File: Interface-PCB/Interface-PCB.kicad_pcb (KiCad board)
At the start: 2 copper layers, 100 x 100 mm, 69 parts, among them IC1 SN74LVC245AN, IC2 TBD62783APG, IC3 TBD62783APG, J1 BARREL_JACK_PAD, J10 LEVEL_SENSOR, J11 TEMPERATURE_SENSOR, J12 TEMPERATURE_SENSOR, J13 CONN_05JST, J14 CONN_05JST, J2 BARREL_JACK_PAD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

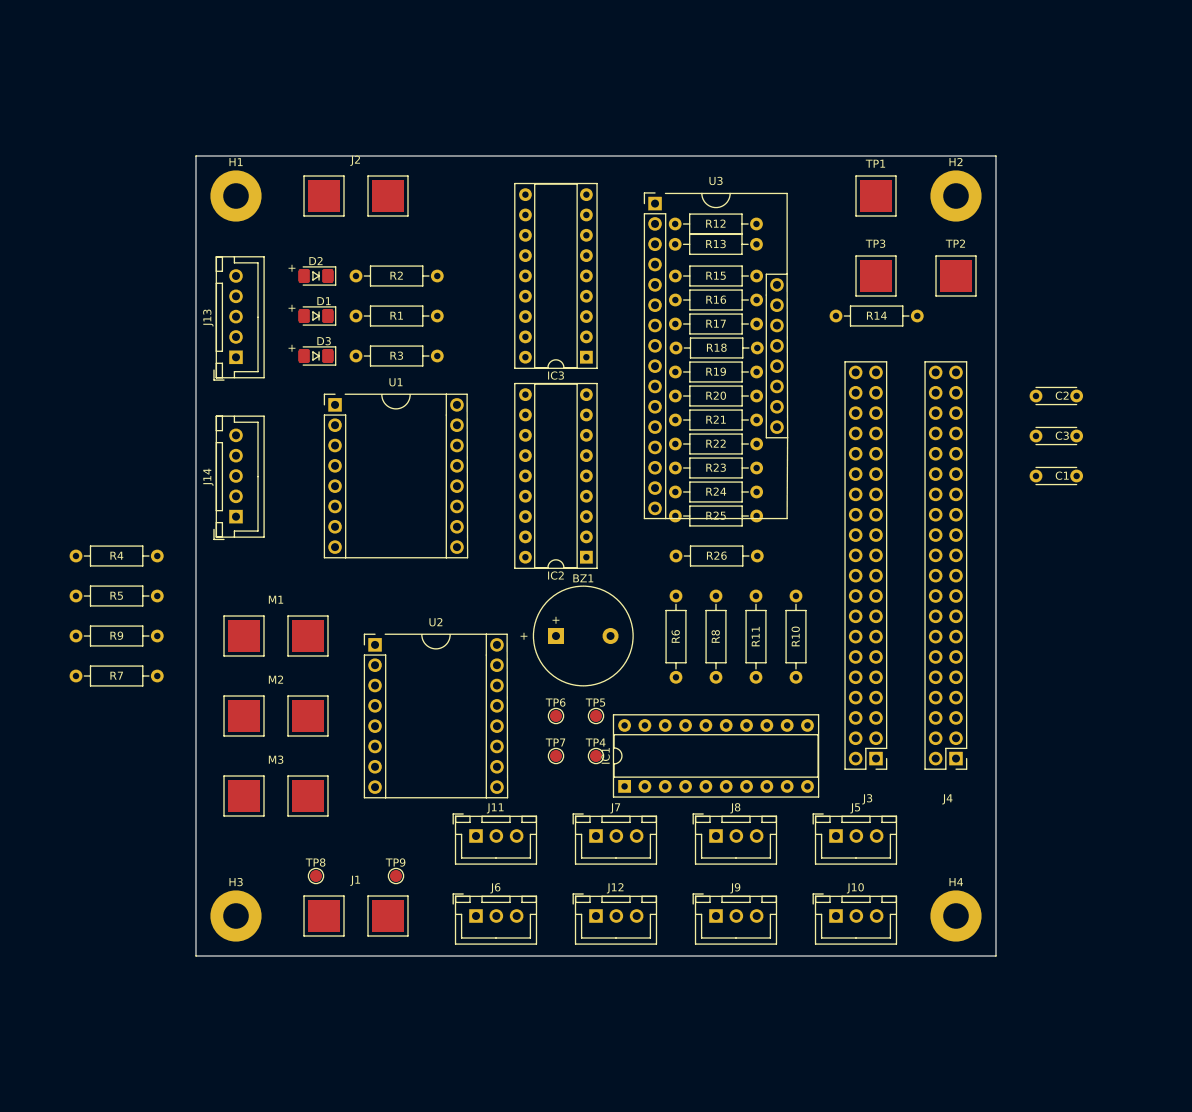
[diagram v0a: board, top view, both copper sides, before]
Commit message: Increase board size, Add connector labels
- Increase board size to 140x130mm
- Refine layout on PCB
- Align breakout board resistors to 2.54mm spacing
- Add Inverted silkscreen labels for off-board connectors
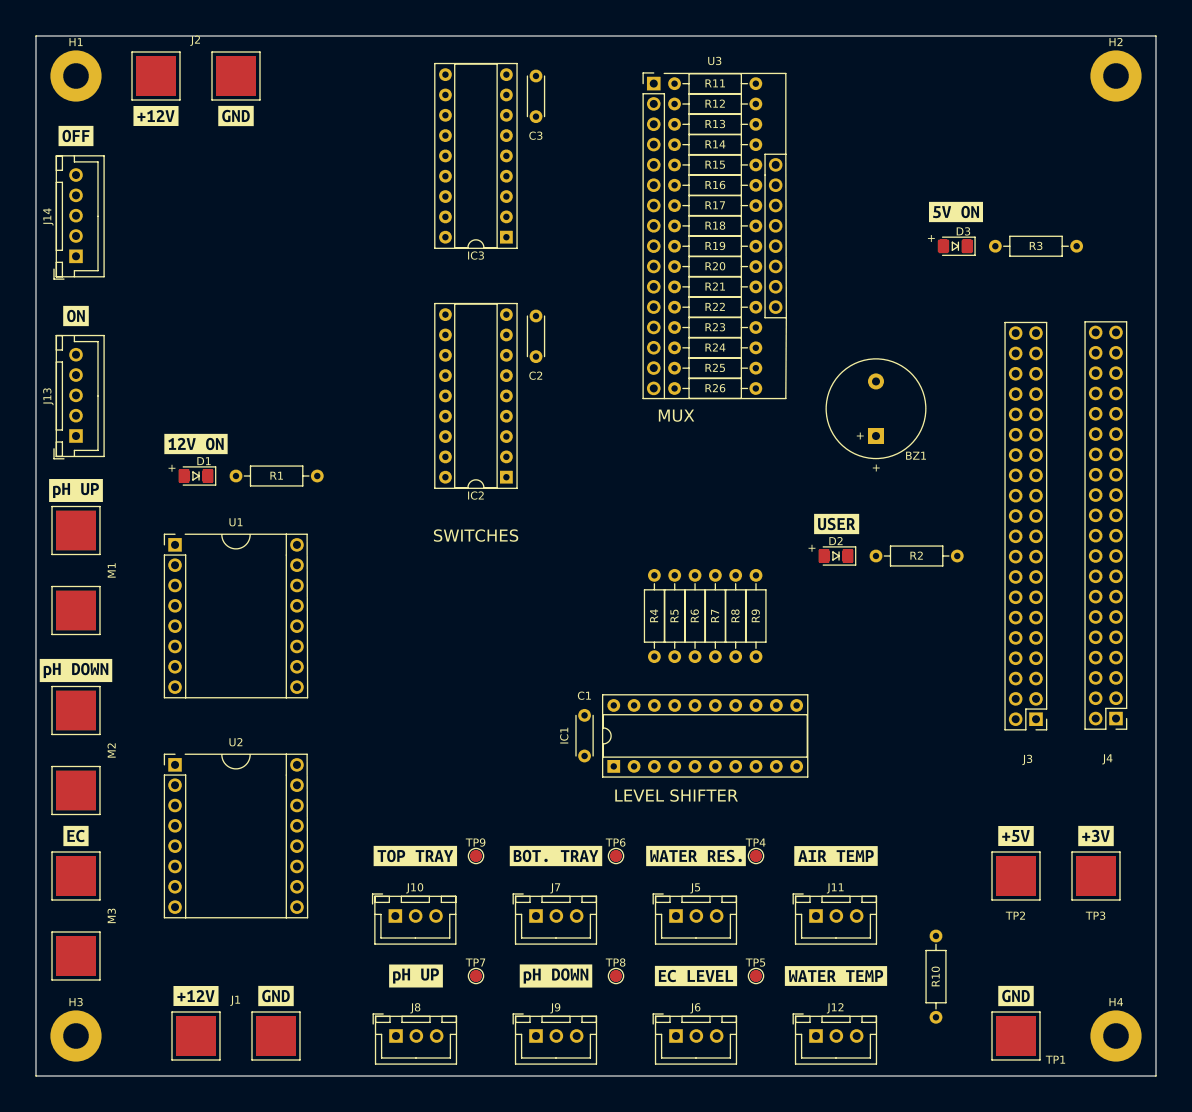
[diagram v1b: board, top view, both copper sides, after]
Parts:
- added kibuzzard-63CB80E4: G***, kibuzzard-63CB80E4, F.Cu at (142.5, 152.5)
- added kibuzzard-63CB8107: G***, kibuzzard-63CB8107, F.Cu at (107.5, 152.5)
- added kibuzzard-63CB8107: G***, kibuzzard-63CB8107, F.Cu at (65.0, 91.8)
- added kibuzzard-63CB811C: G***, kibuzzard-63CB811C, F.Cu at (107.4, 137.5)
- added kibuzzard-63CB8123: G***, kibuzzard-63CB8123, F.Cu at (125.0, 152.5)
- added kibuzzard-63CB8123: G***, kibuzzard-63CB8123, F.Cu at (65.0, 114.3)
- added kibuzzard-63CB8136: G***, kibuzzard-63CB8136, F.Cu at (160.0, 137.5)
- added kibuzzard-63CB813E: G***, kibuzzard-63CB813E, F.Cu at (160.0, 152.5)
- added kibuzzard-63CB8267: G***, kibuzzard-63CB8267, F.Cu at (125.0, 137.5)
- added kibuzzard-63CB83DB: G***, kibuzzard-63CB83DB, F.Cu at (80.0, 86.0)
- added kibuzzard-63CB83FB: G***, kibuzzard-63CB83FB, F.Cu at (175.0, 57.0)
- added kibuzzard-63CB8415: G***, kibuzzard-63CB8415, F.Cu at (160.1, 96.0)
- added kibuzzard-63CB856E: G***, kibuzzard-63CB856E, F.Cu at (65.0, 135.0)
- added kibuzzard-63CB864A: G***, kibuzzard-63CB864A, F.Cu at (182.5, 135.0)
- added kibuzzard-63CB8656: G***, kibuzzard-63CB8656, F.Cu at (192.5, 135.0)
- added kibuzzard-63CB8663: G***, kibuzzard-63CB8663, F.Cu at (182.5, 155.0)
- added kibuzzard-63CB8663: G***, kibuzzard-63CB8663, F.Cu at (90.0, 155.0)
- added kibuzzard-63CB8663: G***, kibuzzard-63CB8663, F.Cu at (85.0, 45.0)
- added kibuzzard-63CB8737: G***, kibuzzard-63CB8737, F.Cu at (80.0, 155.0)
- added kibuzzard-63CB8737: G***, kibuzzard-63CB8737, F.Cu at (75.0, 45.0)
- added kibuzzard-63CB877B: G***, kibuzzard-63CB877B, F.Cu at (142.5, 137.5)
- added kibuzzard-63CB87CD: G***, kibuzzard-63CB87CD, F.Cu at (65.0, 47.5)
- added kibuzzard-63CB87D2: G***, kibuzzard-63CB87D2, F.Cu at (65.0, 70.0)
- J1, J2, M1, M2, M3: footprint AA_Custom_Components:PowerPad_Pair_4.0x4.0mm -> AA_Custom_Components:PowerPad_Pair_5.0x5.0mm
- TP1, TP2, TP3: footprint AA_Custom_Components:TestPoint_Pad_4.0x4.0mm -> AA_Custom_Components:TestPoint_Pad_5.0x5.0mm
- moved TP1 106.4 mm to (182.5, 160.0)
- moved R9 85.0 mm to (150.0, 112.6), turned to 90 degrees
- moved D3 81.1 mm to (174.9, 61.3)
- moved R3 81.1 mm to (179.9, 61.3)
- moved R7 80.9 mm to (144.9, 102.4), turned to -90 degrees
- moved TP3 79.9 mm to (192.5, 140.0)
- moved C3 77.0 mm to (122.5, 40.0), turned to -90 degrees
- moved TP2 75.4 mm to (182.5, 140.0)
- moved R5 74.9 mm to (139.8, 102.4), turned to -90 degrees
- moved D2 73.8 mm to (160.0, 100.0)
- moved R2 73.8 mm to (165.0, 100.0)
- moved R4 73.4 mm to (137.3, 112.6), turned to 90 degrees
- moved C1 66.4 mm to (128.6, 125.0), turned to 90 degrees
- moved R11 64.8 mm to (139.8, 41.0), turned to 0 degrees
- moved C2 63.3 mm to (122.5, 70.0), turned to -90 degrees
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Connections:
- IC1 pad 2: LEVEL_WATER -> LEVEL_TRAY_TOP
- IC1 pad 4: LEVEL_PH_DOWN -> LEVEL_TRAY_BOTTOM
- IC1 pad 5: LEVEL_EC -> LEVEL_PH_DOWN
- IC1 pad 6: LEVEL_TRAY_TOP -> LEVEL_WATER
- IC1 pad 7: LEVEL_TRAY_BOTTOM -> LEVEL_EC
- R4 pad 1: LEVEL_WATER_3V3 -> LEVEL_TRAY_TOP_3V3
- R6 pad 1: LEVEL_PH_DOWN_3V3 -> LEVEL_TRAY_BOTTOM_3V3
- R7 pad 1: LEVEL_EC_3V3 -> LEVEL_PH_DOWN_3V3
- R8 pad 1: LEVEL_TRAY_TOP_3V3 -> LEVEL_WATER_3V3
- R9 pad 1: LEVEL_TRAY_BOTTOM_3V3 -> LEVEL_EC_3V3
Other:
- board size 100 x 100 mm -> 140 x 130 mm
- board text added: "0.1270 mm / 0.1270 mm"
- board text added: "0.2000 mm"
- board text added: "1.6000 mm"
- board text added: "140.0500 mm x 130.0500 mm"
- board text added: "2"
- board text added: "BOARD CHARACTERISTICS"
- board text added: "Board Thickness:"
- board text added: "Board overall dimensions:"
- board text added: "Castellated pads:"
- board text added: "Copper Finish:"
- board text added: "Copper Layer Count:"
- board text added: "Edge card connectors:"
- board text added: "HAL SnPb"
- board text added: "Impedance Control:"
- board text added: "LEVEL SHIFTER"
- board text added: "MUX"
- board text added: "Min hole diameter:"
- board text added: "Min track/spacing:"
- board text added: "No"
- board text added: "Plated Board Edge:"
- board text added: "SWITCHES"

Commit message: Create ground plane, swap motor driver pins
- Create Ground pour/plane on F.Copper
- Swap motor driver pin assignments, to resolve some route
  criss-crossing
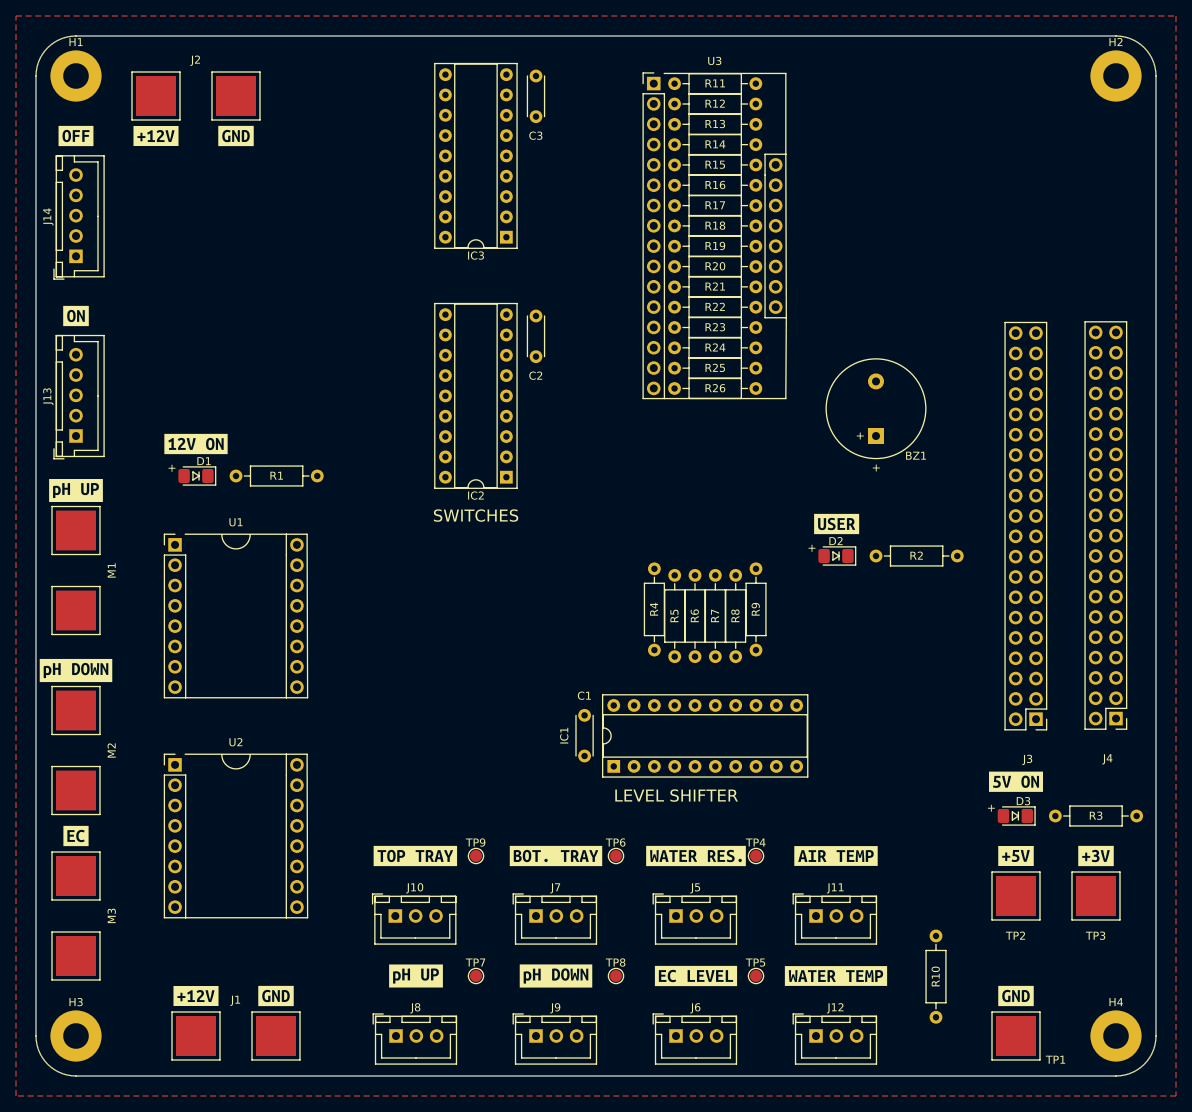
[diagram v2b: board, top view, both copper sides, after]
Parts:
- moved D3 71.6 mm to (182.4, 132.5)
- moved R3 71.6 mm to (187.4, 132.5)
- moved kibuzzard-63CB83FB 71.6 mm to (182.5, 128.2)
- moved R4 11.0 mm to (137.3, 101.6), turned to -90 degrees
- moved R9 11.0 mm to (150.0, 101.6), turned to -90 degrees
- moved J2 2.50 mm to (80.0, 42.5)
- moved TP2 2.50 mm to (182.5, 142.5)
- moved TP3 2.50 mm to (192.5, 142.5)
- moved kibuzzard-63CB864A 2.50 mm to (182.5, 137.5)
- moved kibuzzard-63CB8656 2.50 mm to (192.5, 137.5)
- moved kibuzzard-63CB8663 2.50 mm to (85.0, 47.5)
- moved kibuzzard-63CB8737 2.50 mm to (75.0, 47.5)
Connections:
- J3 pad 11: EN_NUT_2 -> EN_NUT_1
- J3 pad 13: EN_NUT_1 -> EN_NUT_2
- J3 pad 24: EN_DOWN_1 -> EN_DOWN_2
- J3 pad 26: EN_DOWN_2 -> EN_DOWN_1
- J3 pad 38: EN_UP_2 -> EN_UP_1
- J3 pad 40: EN_UP_1 -> EN_UP_2
- J4 pad 11: EN_NUT_2 -> EN_NUT_1
- J4 pad 13: EN_NUT_1 -> EN_NUT_2
- J4 pad 24: EN_DOWN_1 -> EN_DOWN_2
- J4 pad 26: EN_DOWN_2 -> EN_DOWN_1
- J4 pad 38: EN_UP_2 -> EN_UP_1
- J4 pad 40: EN_UP_1 -> EN_UP_2
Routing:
- added copper zone on F.Cu, net GND
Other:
- outline, holes or cut-outs redrawn
- board text removed: "MUX"

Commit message: Align DIP-socket resistors with 2.54mm pin spacing
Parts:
- removed kibuzzard-63CB877B: G***, kibuzzard-63CB877B
- added TP10: GND_PAD, AA_Custom_Components:TestPoint_Pad_5.0x5.0mm, F.Cu at (182.5, 40.0)
- added kibuzzard-63CB8663: G***, kibuzzard-63CB8663, F.Cu at (182.5, 45.0)
- added kibuzzard-63CBAC35: G***, kibuzzard-63CBAC35, F.Cu at (142.5, 137.5)
- moved R2 11.3 mm to (159.8, 110.0)
- moved kibuzzard-63CB8107 10.0 mm to (65.0, 101.8)
- moved kibuzzard-63CB8123 10.0 mm to (65.0, 124.3)
- moved kibuzzard-63CB856E 10.0 mm to (65.0, 145.0)
- moved J2 5.59 mm to (85.0, 40.0)
- moved kibuzzard-63CB8663 5.59 mm to (90.0, 45.0)
- moved kibuzzard-63CB8737 5.59 mm to (80.0, 45.0)
- moved D2 5.51 mm to (162.5, 104.9)
- moved J3 3.76 mm to (181.3, 120.0)
- moved IC1 1.93 mm to (133.7, 125.0)
- moved R5 1.88 mm to (141.3, 101.2)
- moved R6 1.88 mm to (143.8, 101.2)
- moved R7 1.88 mm to (146.3, 101.2)
- moved R8 1.88 mm to (148.9, 101.2)
- moved R9 1.48 mm to (151.4, 101.2)
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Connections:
- net GPIO2_I2C_SDA renamed GPIO2
- net GPIO3_I2C_SCL renamed GPIO3
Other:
- board text added: "GND"
- board text added: "GPIO19"
- board text added: "JLCJLCJLCJLC"
- board text added: "USER"

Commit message: Complete PCB layout
- Complete component positioning and PCB layout
- Swap most pin assignments to resolve track route criss-crossing
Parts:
- removed kibuzzard-63CB83DB: G***, kibuzzard-63CB83DB
- added kibuzzard-63CC577E: G***, kibuzzard-63CC577E, F.Cu at (79.0, 85.0)
- moved kibuzzard-63CB8415 28.8 mm to (167.0, 124.0)
- moved BZ1 27.7 mm to (167.0, 112.6), turned to -90 degrees
- moved R2 25.6 mm to (172.1, 132.5), turned to 180 degrees
- moved D2 23.7 mm to (167.0, 128.2)
- moved IC1 2.64 mm to (133.6, 127.6)
- moved R5 2.64 mm to (141.2, 103.8)
- moved R9 2.64 mm to (151.4, 103.8)
- moved C1 2.64 mm to (129.9, 127.6)
- moved R4 2.64 mm to (138.7, 103.8)
- moved R6 2.64 mm to (143.7, 103.8)
- moved R7 2.64 mm to (146.3, 103.8)
- moved R8 2.64 mm to (148.8, 103.8)
- moved U2 2.50 mm to (85.0, 137.5)
- moved D1 1.41 mm to (79.0, 89.0)
- moved R1 1.41 mm to (84.0, 89.0)
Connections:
- net WATER_TEMP_DATA renamed WATER_TEMP
- J11 pad 2: AIR_TEMP_DATA -> AIR_TEMP
- J3 pad 10: MUX_SEL0 -> EN_NUT_1
- J3 pad 11: EN_NUT_1 -> EN_NUT_2
- J3 pad 12: GPIO18 -> PWM0
- J3 pad 13: EN_NUT_2 -> USER_LED_BUZZER
- J3 pad 15: LEVEL_WATER_3V3 -> LEVEL_EC_3V3
- J3 pad 16: MUX_SEL1 -> LEVEL_WATER_3V3
- J3 pad 18: MUX_SEL2 -> LEVEL_PH_DOWN_3V3
- J3 pad 19: LEVEL_PH_UP_3V3 -> LEVEL_TRAY_BOTTOM_3V3
- J3 pad 21: LEVEL_PH_DOWN_3V3 -> LEVEL_PH_UP_3V3
- J3 pad 22: MUX_SEL3 -> LEVEL_TRAY_TOP_3V3
- J3 pad 23: LEVEL_EC_3V3 -> EN_DOWN_2
- J3 pad 24: EN_DOWN_2 -> EN_DOWN_1
- J3 pad 26: EN_DOWN_1 -> EN_UP_1
- J3 pad 29: LEVEL_TRAY_TOP_3V3 -> EN_UP_2
- J3 pad 31: LEVEL_TRAY_BOTTOM_3V3 -> MUX_EN
- J3 pad 32: PWM0 -> GPIO12
- J3 pad 36: AIR_TEMP_DATA -> MUX_SEL0
- J3 pad 37: USER_LED_BUZZER -> MUX_SEL2
- J3 pad 38: EN_UP_1 -> MUX_SEL1
- J3 pad 40: EN_UP_2 -> MUX_SEL3
- J3 pad 8: MUX_EN -> AIR_TEMP
- J4 pad 10: MUX_SEL0 -> EN_NUT_1
- J4 pad 11: EN_NUT_1 -> EN_NUT_2
- J4 pad 12: GPIO18 -> PWM0
- J4 pad 13: EN_NUT_2 -> USER_LED_BUZZER
- J4 pad 15: LEVEL_WATER_3V3 -> LEVEL_EC_3V3
- J4 pad 16: MUX_SEL1 -> LEVEL_WATER_3V3
- J4 pad 18: MUX_SEL2 -> LEVEL_PH_DOWN_3V3
- J4 pad 19: LEVEL_PH_UP_3V3 -> LEVEL_TRAY_BOTTOM_3V3
- J4 pad 21: LEVEL_PH_DOWN_3V3 -> LEVEL_PH_UP_3V3
- J4 pad 22: MUX_SEL3 -> LEVEL_TRAY_TOP_3V3
- J4 pad 23: LEVEL_EC_3V3 -> EN_DOWN_2
- J4 pad 24: EN_DOWN_2 -> EN_DOWN_1
- J4 pad 26: EN_DOWN_1 -> EN_UP_1
- J4 pad 29: LEVEL_TRAY_TOP_3V3 -> EN_UP_2
- J4 pad 31: LEVEL_TRAY_BOTTOM_3V3 -> MUX_EN
- J4 pad 32: PWM0 -> GPIO12
- J4 pad 36: AIR_TEMP_DATA -> MUX_SEL0
- J4 pad 37: USER_LED_BUZZER -> MUX_SEL2
- J4 pad 38: EN_UP_1 -> MUX_SEL1
- J4 pad 40: EN_UP_2 -> MUX_SEL3
- J4 pad 8: MUX_EN -> AIR_TEMP
- U1 pad 15: PWM0 -> PWM1
- U1 pad 9: PWM0 -> PWM1
- U2 pad 15: PWM1 -> PWM0
- U2 pad 9: PWM1 -> PWM0
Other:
- board text added: "NO"
- board text removed: "GPIO19"

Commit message: Update Blue LED resistor value
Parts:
- R2: value 100 -> 22
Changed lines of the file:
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@@
       (effects (font (size 1 1) (thickness 0.15)))
     )
-    (fp_text value "100" (at 5.08 2.37) (layer "F.Fab")
+    (fp_text value "22" (at 5.08 2.37) (layer "F.Fab")
       (effects (font (size 1 1) (thickness 0.15)))
     )
@@
     (attr board_only exclude_from_pos_files exclude_from_bom)
     (fp_text reference "kibuzzard-63CC577E" (at 0 -4.313238) (layer "F.SilkS") hide
-      (effects (font (size 0 0)))
+      (effects (font (size 0 0) (thickness 0.15)))
     )
     (fp_text value "G***" (at 0 4.313238) (layer "F.SilkS") hide
-      (effects (font (size 0 0)))
+      (effects (font (size 0 0) (thickness 0.15)))
     )
     (fp_poly (pts
